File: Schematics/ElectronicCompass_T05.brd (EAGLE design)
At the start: 50.5 x 50.8 mm, 61 parts, among them Q1 FDN360P, Q2 FDN360P, Q3 FDN360P, Q4 FDN360P, U1 ATMEGA32U4, X1 USBSMD, Y1 16MHz

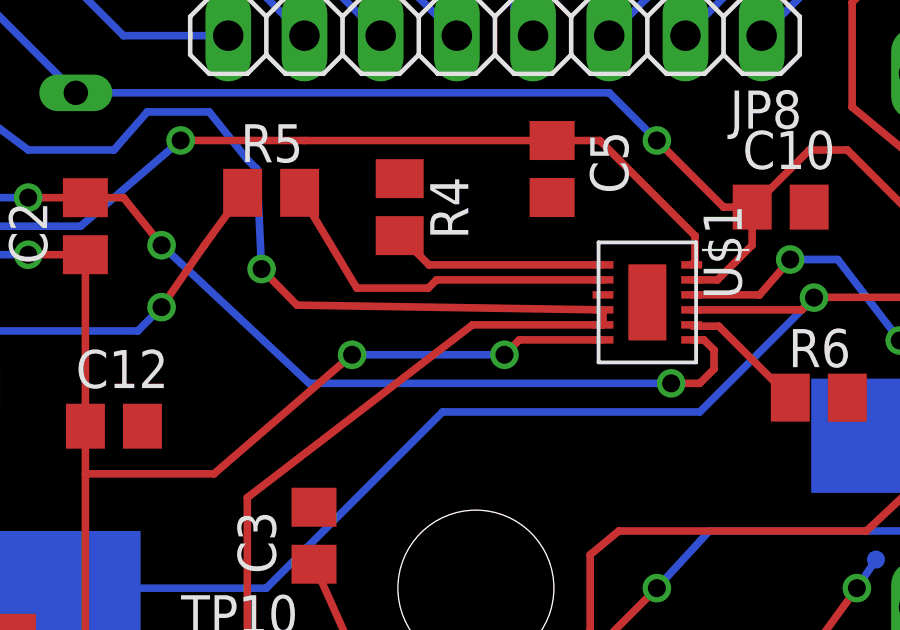
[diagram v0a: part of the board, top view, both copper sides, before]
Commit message: Grounded current limiting programming pins on PMIC
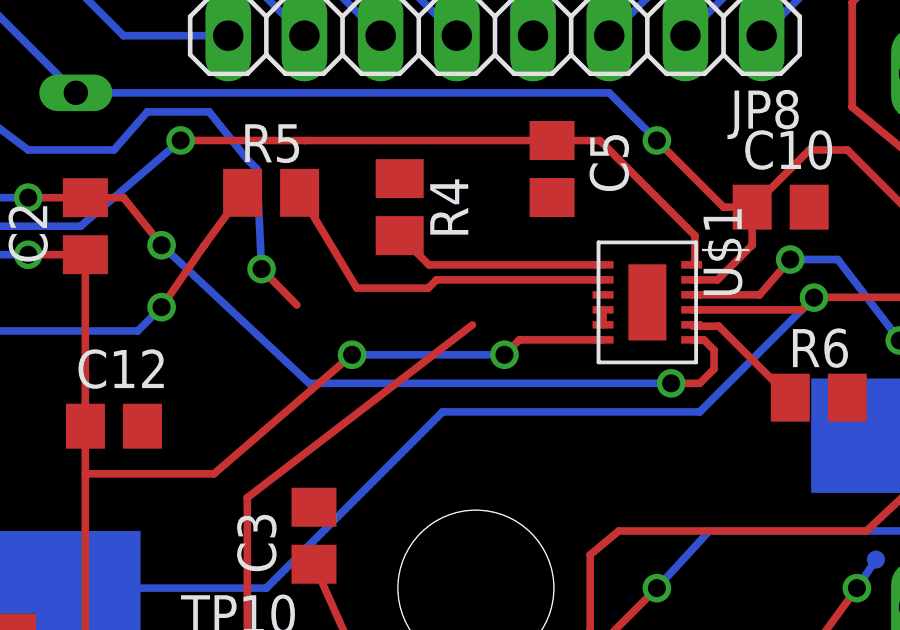
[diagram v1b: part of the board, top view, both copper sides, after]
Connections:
- net GND: now also U$1.P4, U$1.P5
- net VCC: no longer U$1.P4, U$1.P5
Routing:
- net VCC: track 110.7 -> 95.6 mm
- net GND: track 0.00 -> 0.50 mm
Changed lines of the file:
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@@
 <contactref element="U$1" pad="P3"/>
 <contactref element="U$1" pad="P13"/>
+<contactref element="U$1" pad="P5"/>
+<contactref element="U$1" pad="P4"/>
+<wire x1="29.003" y1="36.08" x2="29.003" y2="36.58" width="0.254" layer="1"/>
+<wire x1="35.875" y1="40.005" x2="44.45" y2="44.45" width="0" layer="19" extent="1-1"/>
+<wire x1="30.48" y1="36.83" x2="35.875" y2="40.005" width="0" layer="19" extent="1-1"/>
+<wire x1="29.003" y1="37.08" x2="30.48" y2="36.83" width="0" layer="19" extent="1-1"/>
+<wire x1="29.003" y1="36.58" x2="29.003" y2="37.08" width="0" layer="19" extent="1-1"/>
+<wire x1="27.305" y1="40.325" x2="29.003" y2="37.08" width="0" layer="19" extent="1-1"/>
+<wire x1="22.225" y1="40.955" x2="27.305" y2="40.325" width="0" layer="19" extent="1-1"/>
+<wire x1="37.145" y1="33.655" x2="35.875" y2="40.005" width="0" layer="19" extent="1-1"/>
+<wire x1="38.354" y1="32.385" x2="37.145" y2="33.655" width="0" layer="19" extent="1-16"/>
+<wire x1="46.99" y1="26.67" x2="38.354" y2="32.385" width="0" layer="19" extent="16-16"/>
+<wire x1="19.3675" y1="30.00125" x2="22.225" y2="40.955" width="0" layer="19" extent="1-1"/>
+<wire x1="13.65" y1="32.7025" x2="19.3675" y2="30.00125" width="0" layer="19" extent="1-1"/>
+<wire x1="6.3525" y1="33.9725" x2="13.65" y2="32.7025" width="0" layer="19" extent="1-1"/>
+<wire x1="24.035" y1="18.79875" x2="19.3675" y2="30.00125" width="0" layer="19" extent="1-1"/>
+<wire x1="22.635" y1="15.89875" x2="24.035" y2="18.79875" width="0" layer="19" extent="1-1"/>
+<wire x1="28.035" y1="18.79875" x2="24.035" y2="18.79875" width="0" layer="19" extent="1-1"/>
 <wire x1="29.435" y1="17.89875" x2="28.035" y2="18.79875" width="0" layer="19" extent="1-1"/>
-<wire x1="29.003" y1="37.08" x2="30.48" y2="36.83" width="0" layer="19" extent="1-1"/>
-<wire x1="24.035" y1="18.79875" x2="28.035" y2="18.79875" width="0" layer="19" extent="1-1"/>
-<wire x1="22.635" y1="15.89875" x2="24.035" y2="18.79875" width="0" layer="19" extent="1-1"/>
 <wire x1="25.035" y1="11.99875" x2="22.635" y2="15.89875" width="0" layer="19" extent="1-1"/>
 <wire x1="29.435" y1="12.89875" x2="25.035" y2="11.99875" width="0" layer="19" extent="1-1"/>
-<wire x1="35.875" y1="40.005" x2="30.48" y2="36.83" width="0" layer="19" extent="1-1"/>
-<wire x1="13.65" y1="32.7025" x2="19.3675" y2="30.00125" width="0" layer="19" extent="1-1"/>
+<wire x1="16.98875" y1="14.9225" x2="22.635" y2="15.89875" width="0" layer="19" extent="1-1"/>
+<wire x1="16.66875" y1="9.98625" x2="16.98875" y2="14.9225" width="0" layer="19" extent="1-1"/>
+<wire x1="12.3975" y1="6.19125" x2="16.66875" y2="9.98625" width="0" layer="19" extent="1-1"/>
+<wire x1="12.385" y1="3.33375" x2="12.3975" y2="6.19125" width="0" layer="19" extent="1-16"/>
+<wire x1="29.21" y1="6.35" x2="29.435" y2="12.89875" width="0" layer="19" extent="1-1"/>
+<wire x1="31.75" y1="6.35" x2="29.21" y2="6.35" width="0" layer="19" extent="1-1"/>
+<wire x1="8.85" y1="19.355" x2="16.98875" y2="14.9225" width="0" layer="19" extent="1-1"/>
+<wire x1="6.985" y1="15.875" x2="8.85" y2="19.355" width="0" layer="19" extent="1-16"/>
+<wire x1="48.2575" y1="5.08" x2="31.75" y2="6.35" width="0" layer="19" extent="16-16"/>
 </signal>
 <signal name="VCC">
@@
 <contactref element="S2" pad="2"/>
 <contactref element="Q4" pad="2"/>
-<contactref element="U$1" pad="P5"/>
-<contactref element="U$1" pad="P4"/>
 <wire x1="42.86" y1="7.45" x2="44.28" y2="7.45" width="0.254" layer="16"/>
 <wire x1="44.28" y1="7.45" x2="44.45" y2="7.46125" width="0.254" layer="16"/>
 <wire x1="46.04" y1="7.45" x2="44.62" y2="7.45" width="0.254" layer="1"/>
 <wire x1="44.62" y1="7.45" x2="44.45" y2="7.46125" width="0.254" layer="1"/>
-<wire x1="29.003" y1="36.58" x2="18.8" y2="36.73875" width="0.254" layer="1"/>
 <via x="44.45" y="7.46125" extent="1-16" drill="0.6"/>
 <wire x1="23.535" y1="18.79875" x2="23.535" y2="17.89875" width="0.254" layer="1"/>
@@
 <wire x1="24.535" y1="12.62875" x2="25.55875" y2="13.6525" width="0.254" layer="1"/>
 <wire x1="25.55875" y1="13.6525" x2="28.41625" y2="13.6525" width="0.254" layer="1"/>
-<wire x1="29.003" y1="36.08" x2="29.003" y2="36.58" width="0.254" layer="1"/>
-<wire x1="29.003" y1="36.08" x2="24.65" y2="36.08" width="0.254" layer="1"/>
 <wire x1="23.535" y1="18.79875" x2="23.535" y2="19.16875" width="0.254" layer="1"/>
 <wire x1="23.535" y1="19.16875" x2="22.38375" y2="19.20875" width="0.254" layer="1"/>
@@
 <wire x1="29.435" y1="13.39875" x2="40.005" y2="13.49375" width="0.254" layer="1"/>
 <via x="40.005" y="13.49375" extent="1-16" drill="0.6"/>
+<wire x1="24.65" y1="36.08" x2="18.8" y2="36.73875" width="0" layer="19" extent="1-1"/>
 </signal>
 <signal name="AREF">

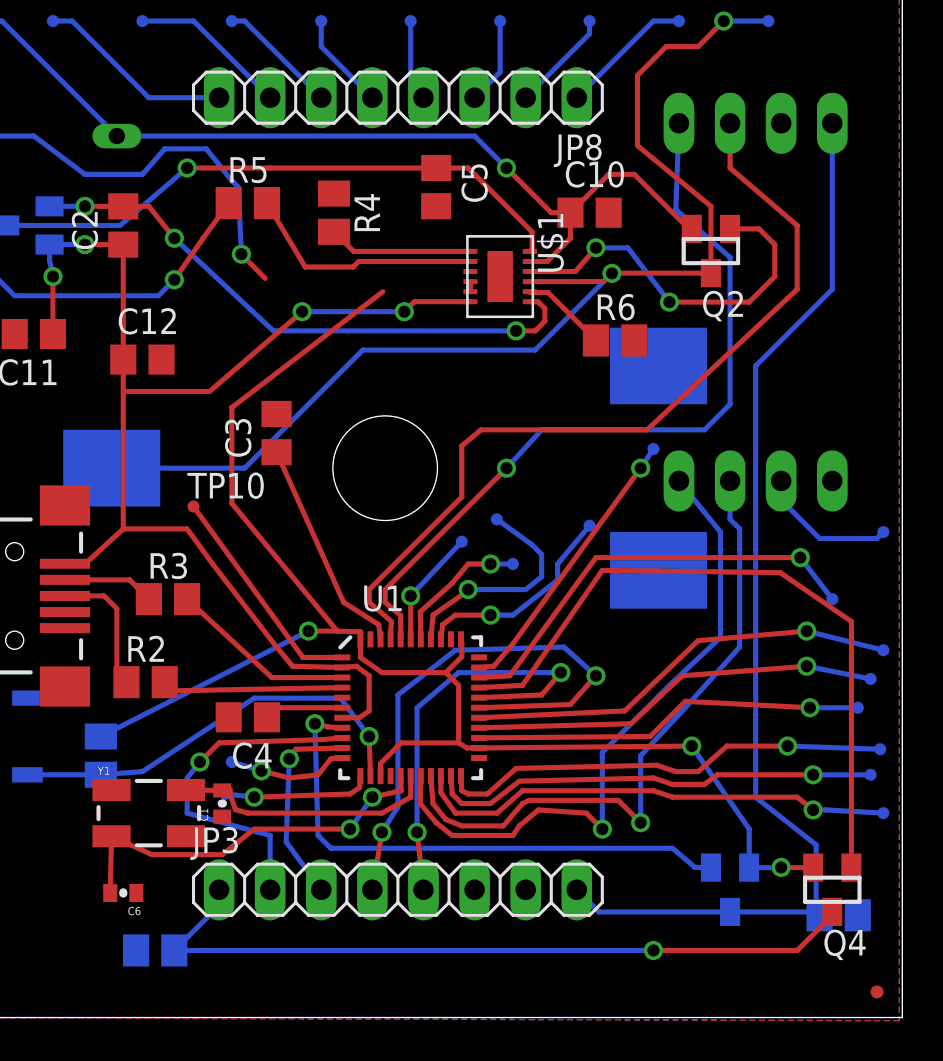
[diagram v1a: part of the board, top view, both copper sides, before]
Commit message: Made some changes to the schematic recommended by Andrew. It is not finished yet but there are some major changes that need to be done before we turn this thing in.
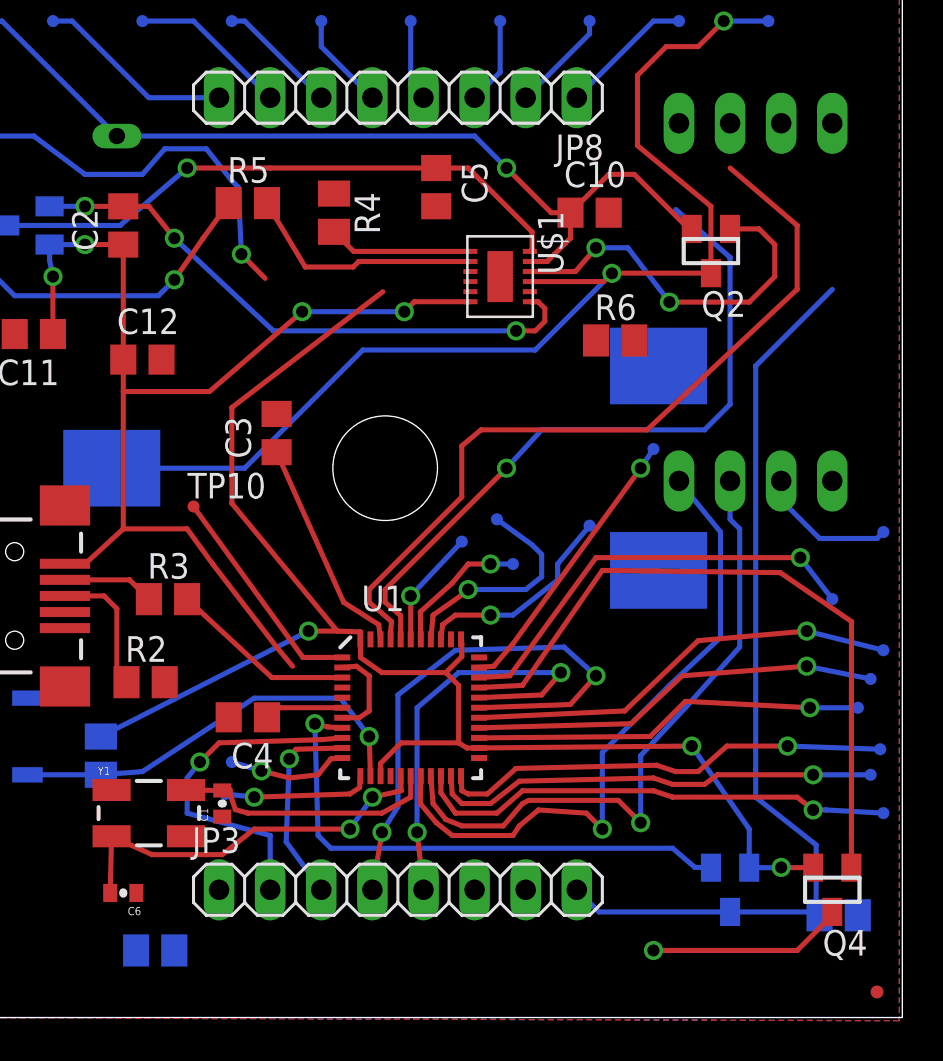
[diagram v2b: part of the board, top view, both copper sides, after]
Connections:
- net D+ renamed N$34
- net N$11 renamed VBUS
- net N$34 renamed DRDY
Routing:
- net LCD_BKLT: track 37.5 -> 10.6 mm
- net N$34: track 9.01 -> 0.00 mm
- net VCC': track 54.8 -> 46.6 mm
- net N$1: track 4.29 -> 0.00 mm
- net INT1: track 39.0 -> 34.7 mm
- net VBUS: track 63.7 -> 61.2 mm
- net INT2: track 41.5 -> 39.3 mm
- net GND: track 0.50 -> 0.00 mm
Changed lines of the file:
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@@
 <contactref element="JP3" pad="6"/>
 <contactref element="JP1" pad="4"/>
-<contactref element="JP2" pad="3"/>
-<contactref element="C5" pad="2"/>
 <contactref element="C11" pad="2"/>
 <contactref element="C3" pad="2"/>
@@
 <contactref element="C6" pad="1"/>
 <contactref element="C1" pad="1"/>
+<contactref element="U$1" pad="P13"/>
+<contactref element="U$1" pad="P4"/>
+<contactref element="JP2" pad="3"/>
+<contactref element="U$1" pad="P5"/>
 <contactref element="U$1" pad="P3"/>
-<contactref element="U$1" pad="P13"/>
-<contactref element="U$1" pad="P5"/>
-<contactref element="U$1" pad="P4"/>
-<wire x1="29.003" y1="36.08" x2="29.003" y2="36.58" width="0.254" layer="1"/>
+<contactref element="C5" pad="2"/>
 <wire x1="35.875" y1="40.005" x2="44.45" y2="44.45" width="0" layer="19" extent="1-1"/>
 <wire x1="30.48" y1="36.83" x2="35.875" y2="40.005" width="0" layer="19" extent="1-1"/>
-<wire x1="29.003" y1="37.08" x2="30.48" y2="36.83" width="0" layer="19" extent="1-1"/>
-<wire x1="29.003" y1="36.58" x2="29.003" y2="37.08" width="0" layer="19" extent="1-1"/>
+<wire x1="29.003" y1="36.58" x2="30.48" y2="36.83" width="0" layer="19" extent="1-1"/>
+<wire x1="29.003" y1="36.08" x2="29.003" y2="36.58" width="0" layer="19" extent="1-1"/>
+<wire x1="29.003" y1="37.08" x2="29.003" y2="36.58" width="0" layer="19" extent="1-1"/>
 <wire x1="27.305" y1="40.325" x2="29.003" y2="37.08" width="0" layer="19" extent="1-1"/>
 <wire x1="22.225" y1="40.955" x2="27.305" y2="40.325" width="0" layer="19" extent="1-1"/>
@@
 <via x="23.97125" y="13.97" extent="1-16" drill="0.6"/>
 </signal>
-<signal name="D+">
-<contactref element="U1" pad="4"/>
-<contactref element="R2" pad="2"/>
-<wire x1="22.635" y1="16.39875" x2="14.2375" y2="16.24" width="0.254" layer="1"/>
-<wire x1="14.2375" y1="16.24" x2="13.80875" y2="16.66875" width="0.254" layer="1"/>
-</signal>
 <signal name="D-">
 <contactref element="U1" pad="3"/>
@@
 </signal>
 <signal name="INT1">
-<contactref element="JP2" pad="1"/>
 <contactref element="U1" pad="40"/>
 <wire x1="25.535" y1="18.79875" x2="25.535" y2="19.97875" width="0.254" layer="1"/>
@@
 <wire x1="24.765" y1="20.6375" x2="24.765" y2="21.2725" width="0.254" layer="1"/>
 <wire x1="24.765" y1="21.2725" x2="30.7975" y2="27.305" width="0.254" layer="1"/>
-<wire x1="39.37" y1="44.45" x2="39.21125" y2="40.16375" width="0.254" layer="16"/>
 <wire x1="39.21125" y1="40.16375" x2="41.91" y2="37.7825" width="0.254" layer="16"/>
 <wire x1="41.91" y1="37.7825" x2="41.91" y2="30.48" width="0.254" layer="16"/>
@@
 <wire x1="32.54375" y1="29.21" x2="30.7975" y2="27.305" width="0.254" layer="16"/>
 <via x="30.7975" y="27.305" extent="1-16" drill="0.6"/>
+<contactref element="JP2" pad="1"/>
+<wire x1="39.21125" y1="40.16375" x2="39.37" y2="44.45" width="0" layer="19" extent="16-16"/>
 </signal>
 <signal name="INT2">
-<contactref element="JP2" pad="2"/>
 <contactref element="U1" pad="41"/>
 <wire x1="25.035" y1="18.79875" x2="25.035" y2="19.16125" width="0.254" layer="1"/>
@@
 <wire x1="28.575" y1="25.87625" x2="28.575" y2="28.41625" width="0.254" layer="1"/>
 <wire x1="28.575" y1="28.41625" x2="29.5275" y2="29.21" width="0.254" layer="1"/>
-<wire x1="41.91" y1="44.45" x2="41.91" y2="42.2275" width="0.254" layer="1"/>
 <wire x1="41.91" y1="42.2275" x2="45.24375" y2="39.37" width="0.254" layer="1"/>
 <wire x1="45.24375" y1="39.37" x2="45.24375" y2="36.195" width="0.254" layer="1"/>
 <wire x1="45.24375" y1="36.195" x2="37.7825" y2="29.21" width="0.254" layer="1"/>
 <wire x1="37.7825" y1="29.21" x2="29.5275" y2="29.21" width="0.254" layer="1"/>
+<contactref element="JP2" pad="2"/>
+<wire x1="41.91" y1="42.2275" x2="41.91" y2="44.45" width="0" layer="19" extent="1-1"/>
 </signal>
 <signal name="VCC'">
 <contactref element="JP3" pad="8"/>
-<contactref element="JP2" pad="4"/>
 <contactref element="R7" pad="2"/>
 <contactref element="Q3" pad="3"/>
@@
 <wire x1="43.18" y1="10.95375" x2="43.18" y2="32.385" width="0.254" layer="16"/>
 <wire x1="43.18" y1="32.385" x2="46.99" y2="36.195" width="0.254" layer="16"/>
-<wire x1="46.99" y1="36.195" x2="46.99" y2="44.45" width="0.254" layer="16"/>
+<contactref element="JP2" pad="4"/>
+<wire x1="46.99" y1="36.195" x2="46.99" y2="44.45" width="0" layer="19" extent="16-16"/>
 </signal>
 <signal name="RESET">
@@
 </signal>
 <signal name="LCD_BKLT">
-<contactref element="R8" pad="2"/>
 <contactref element="JP3" pad="1"/>
 <contactref element="Q4" pad="3"/>
 <wire x1="16.51" y1="6.35" x2="16.51" y2="5.55875" width="0.254" layer="16"/>
-<wire x1="16.51" y1="5.55875" x2="14.285" y2="3.33375" width="0.254" layer="16"/>
-<wire x1="14.285" y1="3.33375" x2="38.1" y2="3.33375" width="0.254" layer="16"/>
 <via x="38.1" y="3.33375" extent="1-16" drill="0.6"/>
 <wire x1="46.99" y1="5.25" x2="46.99" y2="5.08" width="0.254" layer="1"/>
 <wire x1="46.99" y1="5.08" x2="45.24375" y2="3.33375" width="0.254" layer="1"/>
 <wire x1="45.24375" y1="3.33375" x2="38.1" y2="3.33375" width="0.254" layer="1"/>
+<contactref element="R8" pad="2"/>
+<wire x1="16.51" y1="5.55875" x2="38.1" y2="3.33375" width="0" layer="19" extent="16-16"/>
+<wire x1="14.285" y1="3.33375" x2="16.51" y2="5.55875" width="0" layer="19" extent="16-16"/>
 </signal>
 <signal name="N$10">
@@
 <via x="20.0025" y="12.85875" extent="1-16" drill="0.6"/>
 </signal>
-<signal name="N$34">
+<signal name="DRDY">
 <contactref element="JP1" pad="3"/>
 <contactref element="TP18" pad="TP"/>
@@
 <wire x1="41.275" y1="12.065" x2="46.0375" y2="12.065" width="0.254" layer="1"/>
 <via x="46.0375" y="12.065" extent="1-16" drill="0.6"/>
-</signal>
-<signal name="N$1">
-<contactref element="R6" pad="1"/>
-<contactref element="U$1" pad="P8"/>
-<wire x1="35.245" y1="33.655" x2="33.975" y2="34.9225" width="0.254" layer="1"/>
-<wire x1="33.975" y1="34.9225" x2="32.86125" y2="36.03625" width="0.254" layer="1"/>
-<wire x1="32.86125" y1="36.03625" x2="32.00075" y2="36.03625" width="0.254" layer="1"/>
-<wire x1="32.00075" y1="36.03625" x2="31.957" y2="36.08" width="0.254" layer="1"/>
 </signal>
 <signal name="N$4">
@@
 <wire x1="32.22625" y1="34.13125" x2="31.27375" y2="34.13125" width="0.254" layer="1"/>
 </signal>
-<signal name="N$11">
+<signal name="VBUS">
 <contactref element="C11" pad="1"/>
 <contactref element="C2" pad="1"/>
 <contactref element="X1" pad="VBUS"/>
-<contactref element="C12" pad="1"/>
-<contactref element="U1" pad="2"/>
-<contactref element="U1" pad="7"/>
 <contactref element="U$1" pad="P6"/>
 <contactref element="Q1" pad="2"/>
@@
 <wire x1="8.2525" y1="36.51" x2="8.255" y2="36.83" width="0.254" layer="1"/>
 <wire x1="11.7475" y1="38.42" x2="11.7475" y2="32.705" width="0.254" layer="1"/>
-<wire x1="11.7475" y1="32.705" x2="11.75" y2="32.7025" width="0.254" layer="1"/>
 <via x="8.255" y="36.83" extent="1-16" drill="0.6"/>
 <via x="9.8425" y="38.4175" extent="1-16" drill="0.6"/>
@@
 <wire x1="16.1925" y1="22.5425" x2="19.3675" y2="18.415" width="0.254" layer="1"/>
 <wire x1="19.3675" y1="18.415" x2="20.16125" y2="17.4625" width="0.254" layer="1"/>
-<wire x1="22.635" y1="14.89875" x2="23.47125" y2="14.89875" width="0.254" layer="1"/>
-<wire x1="23.47125" y1="14.89875" x2="23.97125" y2="15.24" width="0.254" layer="1"/>
-<wire x1="23.97125" y1="15.24" x2="23.97125" y2="16.98625" width="0.254" layer="1"/>
 <wire x1="29.003" y1="35.58" x2="26.21375" y2="35.58" width="0.254" layer="1"/>
 <wire x1="26.21375" y1="35.58" x2="25.7175" y2="35.08375" width="0.254" layer="1"/>
@@
 <via x="20.6375" y="35.08375" extent="1-16" drill="0.6"/>
 <via x="25.7175" y="35.08375" extent="1-16" drill="0.6"/>
+<contactref element="U1" pad="2"/>
+<contactref element="U1" pad="7"/>
+<wire x1="22.635" y1="14.89875" x2="23.47125" y2="14.89875" width="0.254" layer="1"/>
+<wire x1="23.47125" y1="14.89875" x2="23.97125" y2="15.24" width="0.254" layer="1"/>
+<wire x1="23.97125" y1="15.24" x2="23.97125" y2="16.98625" width="0.254" layer="1"/>
 <wire x1="23.97125" y1="16.98625" x2="23.33625" y2="17.4625" width="0.254" layer="1"/>
-<wire x1="20.16125" y1="17.4625" x2="22.635" y2="17.39875" width="0.254" layer="1"/>
 <wire x1="23.33625" y1="17.4625" x2="22.635" y2="17.39875" width="0.254" layer="1"/>
+<contactref element="C12" pad="1"/>
 <wire x1="11.75" y1="32.7025" x2="11.7475" y2="31.115" width="0" layer="19" extent="1-1"/>
+<wire x1="11.7475" y1="32.705" x2="11.75" y2="32.7025" width="0" layer="19" extent="1-1"/>
+<wire x1="22.635" y1="17.39875" x2="20.16125" y2="17.4625" width="0" layer="19" extent="1-1"/>
 </signal>
 <signal name="N$5">
@@
 <signal name="N$27">
 </signal>
+<signal name="N$34">
+<contactref element="U1" pad="4"/>
+<contactref element="R2" pad="2"/>
+<wire x1="13.80875" y1="16.66875" x2="22.635" y2="16.39875" width="0" layer="19" extent="1-1"/>
+</signal>
+<signal name="N$1">
+<contactref element="U$1" pad="P8"/>
+<contactref element="R6" pad="1"/>
+<wire x1="35.245" y1="33.655" x2="31.957" y2="36.08" width="0" layer="19" extent="1-1"/>
+</signal>
 </signals>
